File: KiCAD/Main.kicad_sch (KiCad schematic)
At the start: 33 parts, among them J1 USB_C_Receptacle_USB2.0_14P, J2 Conn_01x03_Socket, SW1 SW_DIP_x01, U1 RP2040, U2 NCP1117-3.3_SOT223, U3 W25Q16JVSS, Y1 ABM8-272-T3

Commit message: Start PCB Layout
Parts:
- removed TP1: TestPoint, symbol Connector:TestPoint
- J1: footprint (none) -> Fightstick_Library:USB_C_Receptacle_HCTL_Fightstick_16P_TopMnt_Horizontal; symbol Connector:USB_C_Receptacle_USB2.0_14P -> Connector:USB_C_Receptacle_USB2.0_16P
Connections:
- net UP2: now reaches U1.34 (GPIO22)
- net UP renamed UP1
- no-connect marks 0 -> 2
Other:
- note added: "TODO add hardware to chose up buttons modes"
- note added: "TODO figure out the keyswitch footprints"

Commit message: PCB First Draft
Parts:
- removed C17: 100n, Capacitor_SMD:C_0402_1005Metric, symbol Device:C
- J2: footprint (none) -> Fightstick_Library:Debug_Points; now left out of the parts list
- SW1: footprint (none) -> Fightstick_Library:SW_SMD_BUTTON_YTS_A007; symbol Switch:SW_DIP_x01 -> Switch:SW_Push_Shielded
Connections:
- net R3 is gone; now on net S2: U1.30 (GPIO19)
- net RUN is gone; now on net +3.3V: U1.26 (RUN)
- net SLC is gone; now on net L2: U1.3 (GPIO1)
- net TURBO is gone; now on net A2: U1.17 (GPIO14)
- net A1: now also U1.27 (GPIO16); no longer U1.31 (GPIO20)
- net A2: no longer U1.32 (GPIO21)
- net B1: now also U1.9 (GPIO7); no longer U1.8 (GPIO6)
- net B2: now also U1.11 (GPIO8); no longer U1.9 (GPIO7)
- net B4: now also U1.15 (GPIO12); no longer U1.14 (GPIO11)
- net DOWN: now also U1.6 (GPIO4); no longer U1.5 (GPIO3)
- net GND: now also SW1.0 (B)
- net L1: now also U1.28 (GPIO17); no longer U1.16 (GPIO13)
- net L2: no longer U1.12 (GPIO9)
- net L3: now also U1.14 (GPIO11); no longer U1.29 (GPIO18)
- net LEFT: now also U1.5 (GPIO3); no longer U1.7 (GPIO5)
- net R1: now also U1.16 (GPIO13); no longer U1.15 (GPIO12)
- net R2: now also U1.12 (GPIO9); no longer U1.11 (GPIO8)
- net RIGHT: now also U1.7 (GPIO5); no longer U1.6 (GPIO4)
- net S1: now also U1.29 (GPIO18); no longer U1.27 (GPIO16)
- net S2: no longer U1.28 (GPIO17)
- net SDA renamed MODE
- net T LED: no longer names the net of U1.18 (GPIO15)
- net UP1 renamed SPACE
- net UP2: no longer names the net of U1.34 (GPIO22)
- new net W: U1.8 (GPIO6)
- no-connect marks 2 -> 13
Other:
- note added: "One cap near each of pins: 1, 10, 22, 33, 42, 48, 49"
- note added: "Tie RUN pin to IOVDD for now external resets"
- note removed: "One cap near each of pins: 1, 10, 22, 33, 42, 43, 48, 49"
- note removed: "RESET"
- note removed: "TODO put some easy method to short RUN to ground to reset the microcontroller"

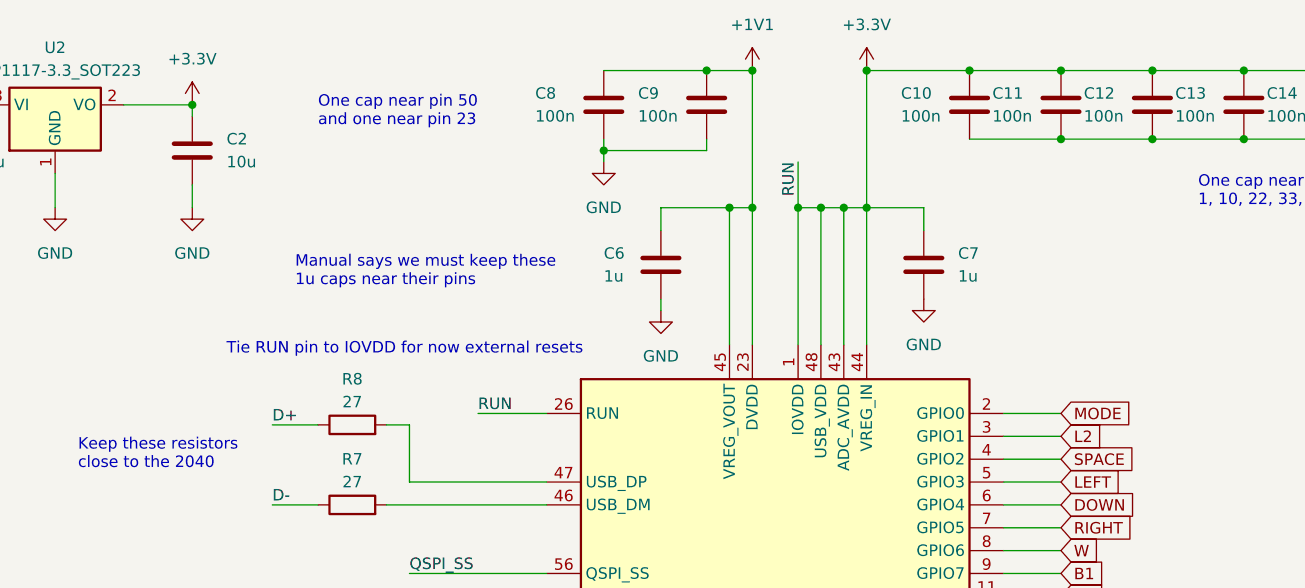
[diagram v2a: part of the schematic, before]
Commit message: Make PCB and case fit together
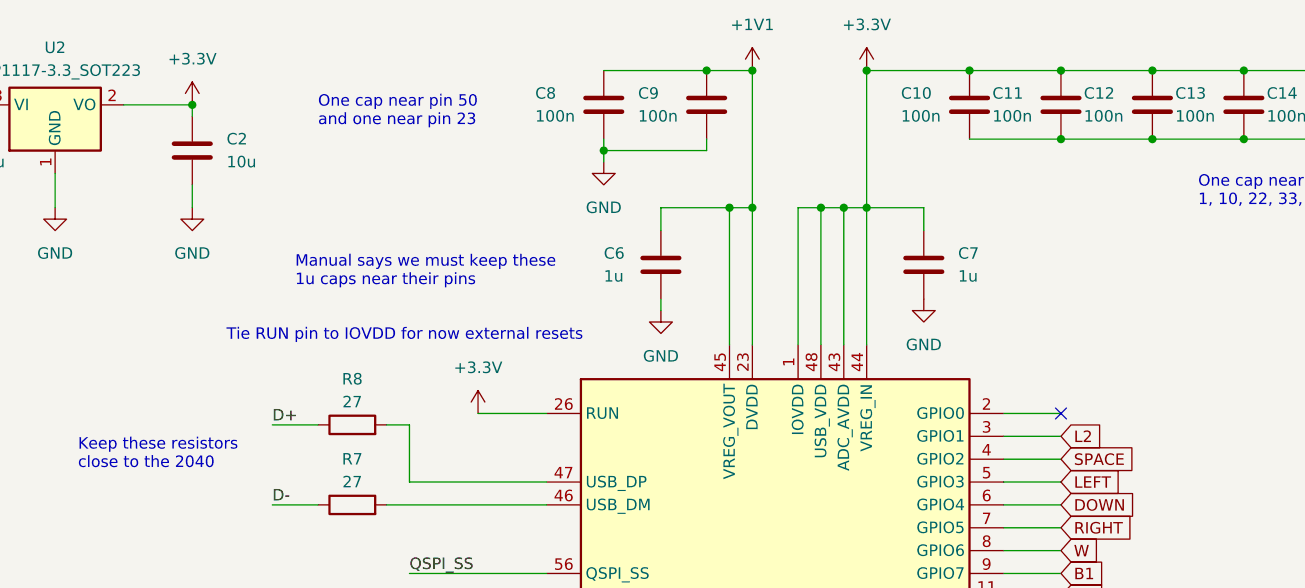
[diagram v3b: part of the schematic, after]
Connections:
- net MODE: no longer names the net of U1.2 (GPIO0)
- no-connect marks 13 -> 14
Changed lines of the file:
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@@
 	)
 	(junction
-		(at 186.69 45.72)
-		(diameter 0)
-		(color 0 0 0 0)
-	)
-	(junction
 		(at 176.53 30.48)
 		(diameter 0)
@@
 	)
 	(no_connect
+		(at 215.9 68.58)
+	)
+	(no_connect
 		(at 215.9 119.38)
 	)
@@
 	(wire
 		(pts
-			(xy 186.69 40.64) (xy 186.69 45.72)
-		)
-		(stroke
-			(width 0)
-			(type default)
-		)
-	)
-	(wire
-		(pts
 			(xy 86.36 101.6) (xy 95.25 101.6)
 		)
@@
 	(text "Tie RUN pin to IOVDD for now external resets"
 		(exclude_from_sim no)
-		(at 143.002 61.468 0)
+		(at 143.002 59.944 0)
 		(effects
 			(font
@@
 		)
 	)
-	(label "RUN"
-		(at 151.13 68.58 0)
-		(fields_autoplaced yes)
-		(effects
-			(font
-				(size 1.27 1.27)
-			)
-			(justify left bottom)
-		)
-	)
 	(label "SWDIO"
 		(at 143.51 137.16 0)
@@
 		)
 	)
-	(label "RUN"
-		(at 186.69 40.64 270)
-		(fields_autoplaced yes)
-		(effects
-			(font
-				(size 1.27 1.27)
-			)
-			(justify right bottom)
-		)
-	)
 	(label "QSPI_SD3"
 		(at 58.42 172.72 0)
@@
 		)
 	)
-	(global_label "MODE"
-		(shape input)
-		(at 215.9 68.58 0)
-		(fields_autoplaced yes)
-		(effects
-			(font
-				(size 1.27 1.27)
-			)
-			(justify left)
-		)
-		(property "Intersheetrefs" "${INTERSHEET_REFS}"
-			(at 224.0861 68.58 0)
-			(effects
-				(font
-					(size 1.27 1.27)
-				)
-				(justify left)
-				(hide yes)
-			)
-		)
-	)
 	(global_label "L2"
 		(shape input)
@@
 					(unit 1)
 				)
+			)
+		)
+	)
+	(symbol
+		(lib_name "+3.3V_1")
+		(lib_id "power:+3.3V")
+		(at 151.13 68.58 0)
+		(unit 1)
+		(exclude_from_sim no)
+		(in_bom yes)
+		(on_board yes)
+		(dnp no)
+		(fields_autoplaced yes)
+		(property "Reference" "#PWR037"
+			(at 151.13 72.39 0)
+			(effects
+				(font
+					(size 1.27 1.27)
+				)
+				(hide yes)
+			)
+		)
+		(property "Value" "+3.3V"
+			(at 151.13 63.5 0)
+			(effects
+				(font
+					(size 1.27 1.27)
+				)
+			)
+		)
+		(property "Footprint" ""
+			(at 151.13 68.58 0)
+			(effects
+				(font
+					(size 1.27 1.27)
+				)
+				(hide yes)
+			)
+		)
+		(property "Datasheet" ""
+			(at 151.13 68.58 0)
+			(effects
+				(font
+					(size 1.27 1.27)
+				)
+				(hide yes)
+			)
+		)
+		(property "Description" "Power symbol creates a global label with name \"+3.3V\""
+			(at 151.13 68.58 0)
+			(effects
+				(font
+					(size 1.27 1.27)
+				)
+				(hide yes)
+			)
+		)
+		(pin "1"
+		)
+		(instances
+			(project ""
+				(path "/d4101bc9-65c8-46ec-b973-5d64e4a94ac0/8c80bd9b-e7f4-4fd2-8937-7b0f564b4108"
+					(reference "#PWR037")
+					(unit 1)
+				)

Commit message: First DFM pass
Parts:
- R6: now left out of the parts list
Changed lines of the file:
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@@
 		(unit 1)
 		(exclude_from_sim no)
-		(in_bom yes)
+		(in_bom no)
 		(on_board yes)
 		(dnp no)

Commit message: Second DFM pass
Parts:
- J1: JLCPCB # (none) -> C6332272
- SW1: JLCPCB # (none) -> C2910660
- U2: JLCPCB # (none) -> C26537
- U3: JLCPCB # (none) -> C131025
- Y1: JLCPCB # (none) -> C20625731
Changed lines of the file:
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@@
+			)
+		)
+		(property "JLCPCB #" "C20625731"
+			(at 43.18 113.03 90)
+			(effects
+				(font
+					(size 1.27 1.27)
+				)
+				(hide yes)
 			)
 		)
@@
 			)
 		)
+		(property "JLCPCB #" "C26537"
+			(at 104.14 34.29 0)
+			(effects
+				(font
+					(size 1.27 1.27)
+				)
+				(hide yes)
+			)
+		)
 		(pin "2"
 		)
@@
 			)
 		)
+		(property "JLCPCB #" "C6332272"
+			(at 30.48 49.53 0)
+			(effects
+				(font
+					(size 1.27 1.27)
+				)
+				(hide yes)
+			)
+		)
 		(pin "B9"
 		)
@@
 		)
 		(property "Description" "Generic push-button switch, two contact pins and shield pin(s)"
+			(at 30.48 160.02 0)
+			(effects
+				(font
+					(size 1.27 1.27)
+				)
+				(hide yes)
+			)
+		)
+		(property "JLCPCB #" "C2910660"
 			(at 30.48 160.02 0)
 			(effects
@@
 			(at 78.74 167.64 0)
 			(effects
+				(font
+					(size 1.27 1.27)
+				)
+				(hide yes)
+			)
+		)
+		(property "JLCPCB #" "C131025"
+			(at 78.74 167.64 0)
+			(effects

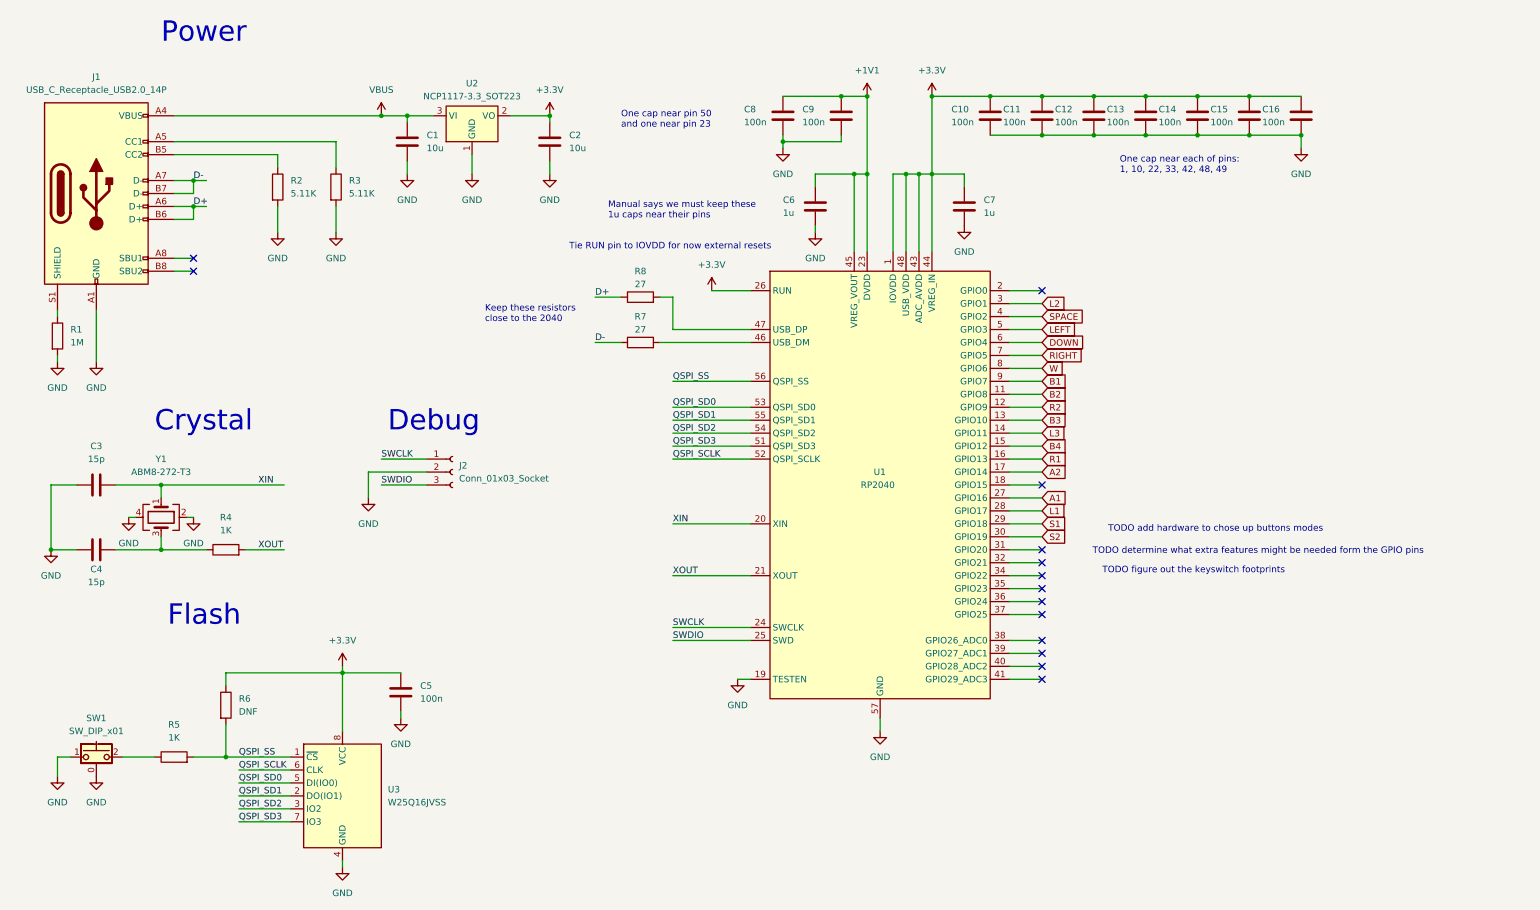
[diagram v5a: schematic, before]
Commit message: Add multiboard configurations
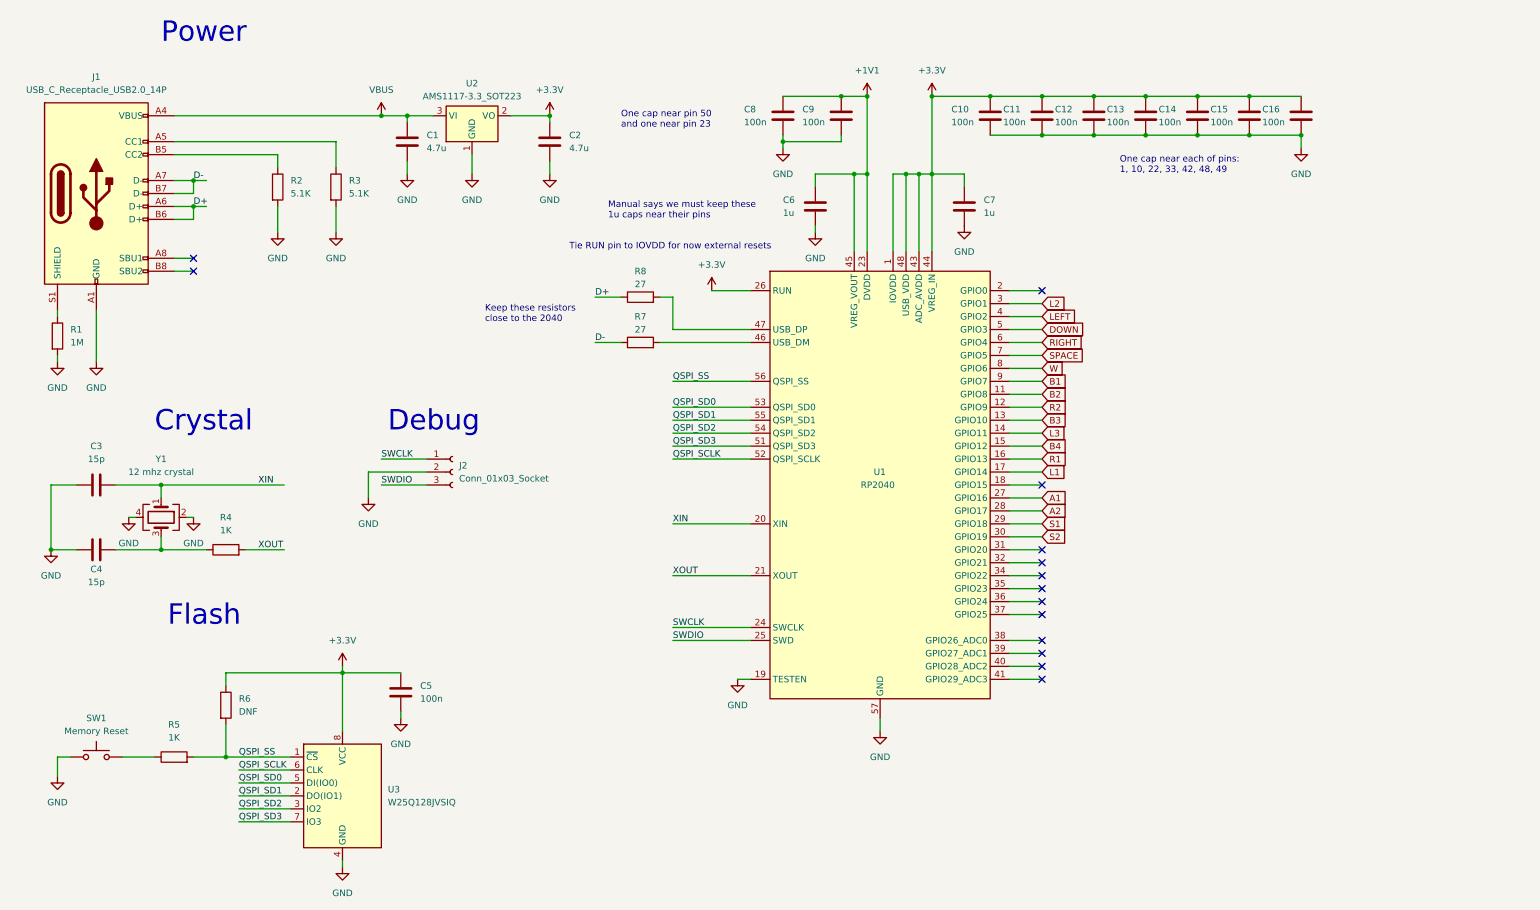
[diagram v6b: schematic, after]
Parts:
- C1, C2: value 10u -> 4.7u; LCSC (none) -> C15525
- C10, C11, C12, C13, C14, C15, C16, C5, C8, C9: LCSC (none) -> C1525
- C3, C4: LCSC (none) -> C1548
- C6, C7: LCSC (none) -> C52923
- J1: footprint Fightstick_Library:USB_C_Receptacle_HCTL_Fightstick_16P_TopMnt_Horizontal -> Leverless_Controller_Library:USB_C_Receptacle_C6332272; JLCPCB # C6332272 -> (none); LCSC (none) -> C6332272
- J2: footprint Fightstick_Library:Debug_Points -> Leverless_Controller_Library:Debug_Points
- R1: LCSC (none) -> C26083
- R2, R3: value 5.11K -> 5.1K; LCSC (none) -> C25905
- R4, R5: LCSC (none) -> C11702
- R7, R8: footprint Resistor_SMD:R_0402_1005Metric -> Resistor_SMD:R_0603_1608Metric; LCSC (none) -> C25190
- SW1: value SW_DIP_x01 -> Memory Reset; footprint Fightstick_Library:SW_SMD_BUTTON_YTS_A007 -> Button_Switch_SMD:SW_SPST_TL3342; symbol Switch:SW_Push_Shielded -> Switch:SW_Push; JLCPCB # C2910660 -> (none); LCSC (none) -> C318884
- U1: LCSC (none) -> C2040
- U2: value NCP1117-3.3_SOT223 -> AMS1117-3.3_SOT223; JLCPCB # C26537 -> (none); LCSC (none) -> C6186
- U3: value W25Q16JVSS -> W25Q128JVSIQ; JLCPCB # C131025 -> (none); LCSC (none) -> C97521
- Y1: value ABM8-272-T3 -> 12 mhz crystal; JLCPCB # C20625731 -> (none); LCSC (none) -> C9002
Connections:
- net A2: now also U1.28 (GPIO17); no longer U1.17 (GPIO14)
- net DOWN: now also U1.5 (GPIO3); no longer U1.6 (GPIO4)
- net GND: no longer SW1.0 (B)
- net L1: now also U1.17 (GPIO14); no longer U1.28 (GPIO17)
- net LEFT: now also U1.4 (GPIO2); no longer U1.5 (GPIO3)
- net RIGHT: now also U1.6 (GPIO4); no longer U1.7 (GPIO5)
- net SPACE: now also U1.7 (GPIO5); no longer U1.4 (GPIO2)
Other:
- note removed: "TODO add hardware to chose up buttons modes"
- note removed: "TODO determine what extra features might be needed form the GPIO pins"
- note removed: "TODO figure out the keyswitch footprints"
